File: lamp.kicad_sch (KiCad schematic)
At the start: 18 parts, among them J1 Screw_Terminal_01x02, J2 Screw_Terminal_01x02, Q1 2N7002, U1 ESP-12E, U2 34.81-7048, U3 AMS1117-3.3

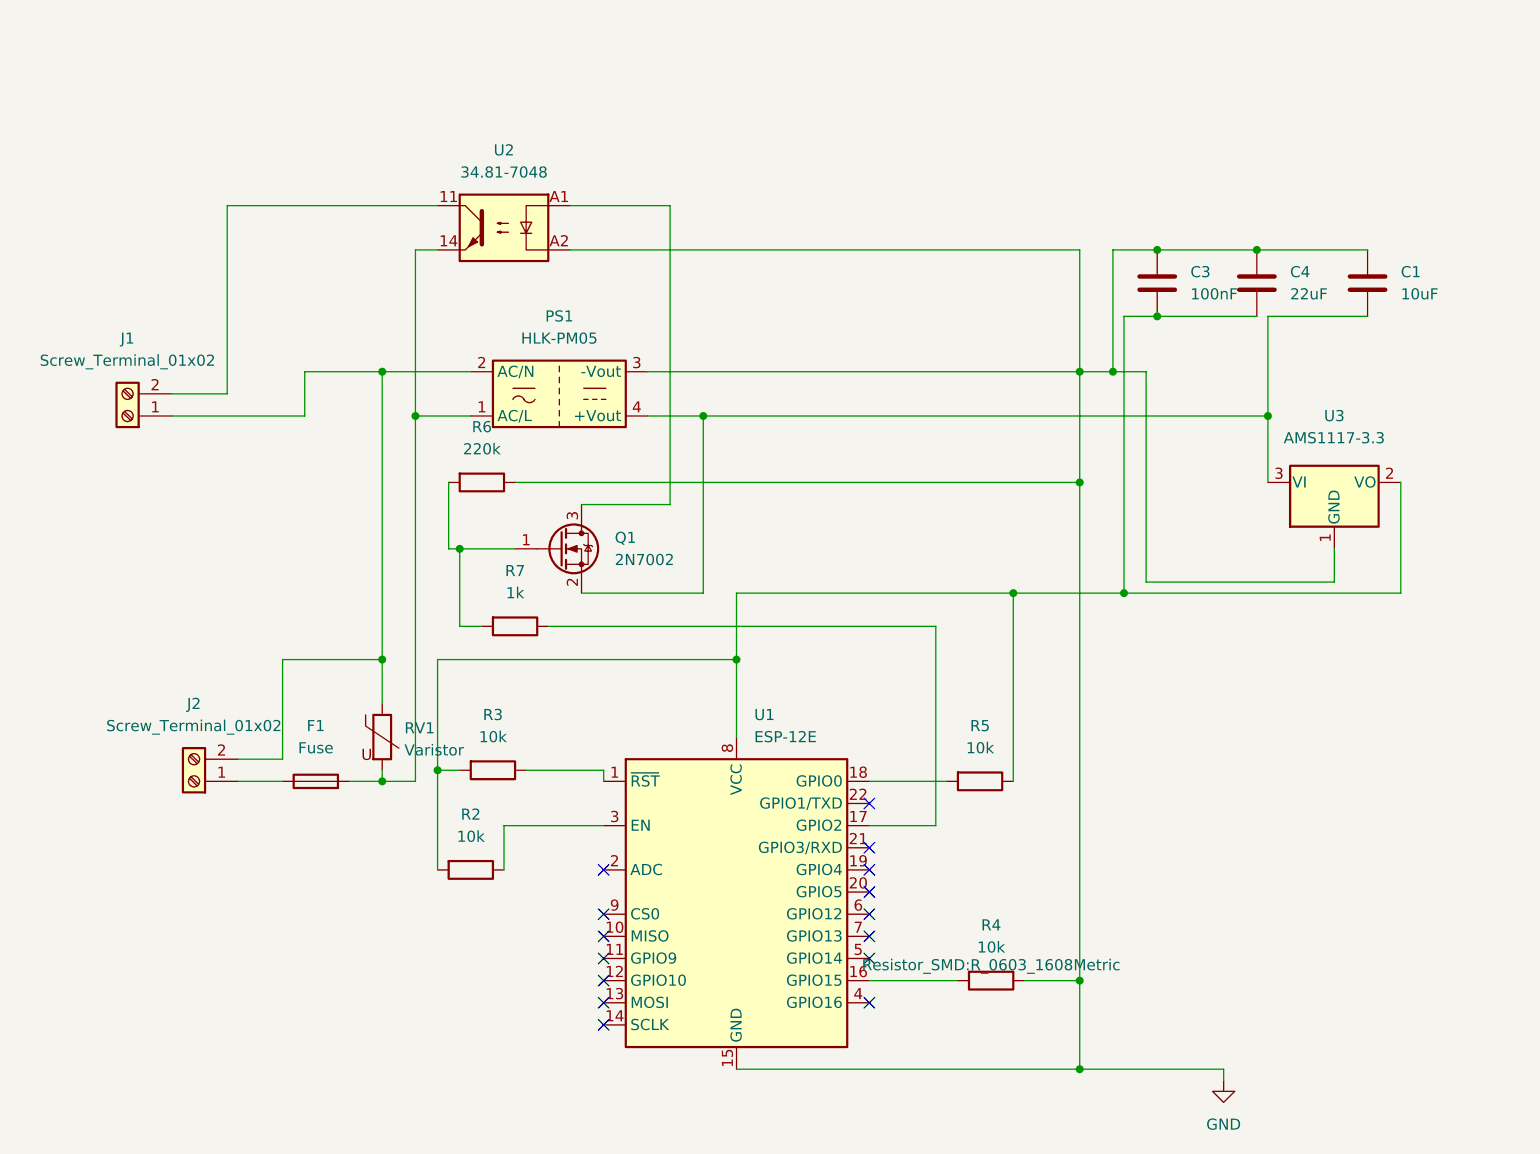
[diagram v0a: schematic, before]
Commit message: 0.1 revision
broken tracing
fixed capacitor footprint
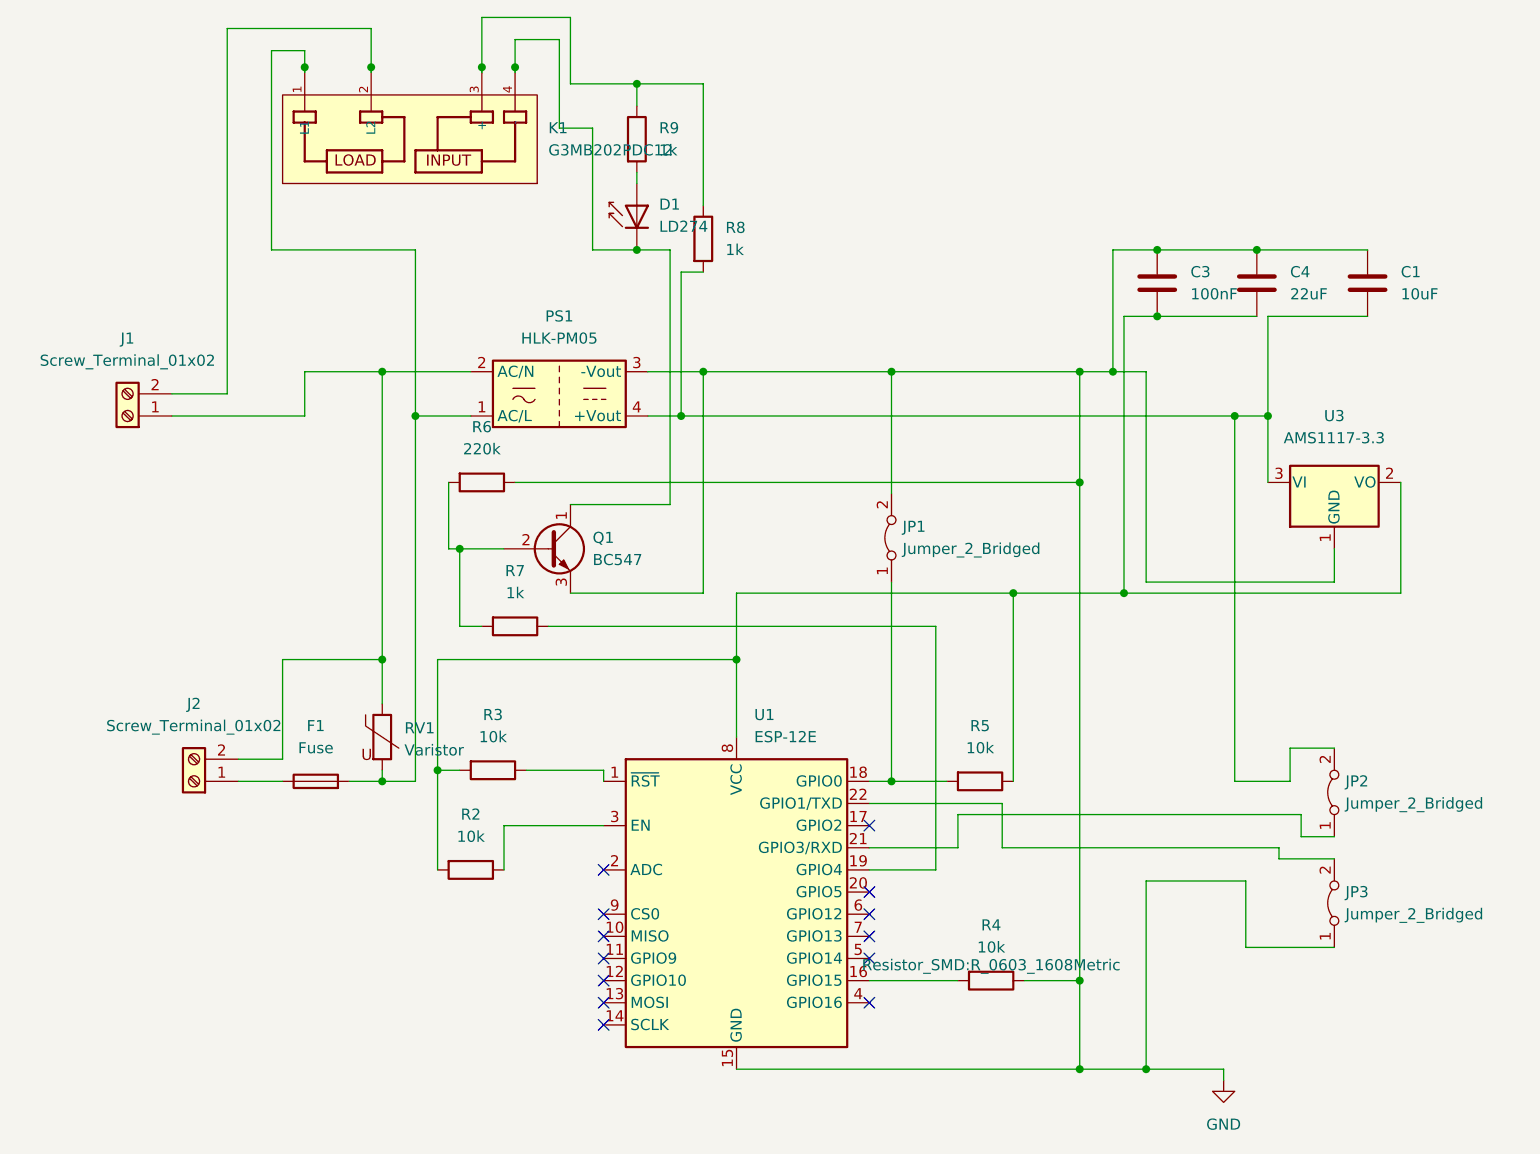
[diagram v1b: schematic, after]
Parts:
- removed Q1: 2N7002, Package_TO_SOT_SMD:SOT-23, symbol Transistor_FET:2N7002
- removed U2: 34.81-7048, OptoDevice:Finder_34.81, symbol Relay_SolidState:34.81-7048
- added D1: LD274, LED_THT:LED_D5.0mm_IRGrey, symbol LED:LD274
- added JP1, JP2, JP3: Jumper_2_Bridged, TestPoint:TestPoint_2Pads_Pitch2.54mm_Drill0.8mm, symbol Jumper:Jumper_2_Bridged
- added K1: G3MB202PDC12, G3MB202PDC12:RELAY_G3MB202PDC12, symbol G3MB202PDC12:G3MB202PDC12
- added Q1: BC547, Package_TO_SOT_THT:TO-92_Inline, symbol Transistor_BJT:BC547
- added R8, R9: 1k, Resistor_SMD:R_0603_1608Metric, symbol Device:R
- C1, C3, C4: footprint Capacitor_Tantalum_SMD:CP_EIA-3216-18_Kemet-A_Pad1.58x1.35mm_HandSolder -> Capacitor_THT:CP_Radial_D5.0mm_P2.50mm
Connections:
- net GND: now also JP1.2 (B), JP3.1 (A), Q1.3 (E)
- net at F1.2, PS1.1 (AC/L), RV1.2: now also K1.1 (L1)
- net at C1.2, PS1.4 (+Vout), U3.3 (VI): now also JP2.2 (B), R8.2
- net at R5.2, U1.18 (GPIO0): now also JP1.1 (A)
- net at J1.2 (Pin_2): now also K1.2 (L2)
- net at R7.1: now also U1.19 (GPIO4); no longer U1.17 (GPIO2)
- net at R6.2, R7.2: now also Q1.2 (B)
- net at U1.21 (GPIO3/RXD): now also JP2.1 (A)
- net at U1.22 (GPIO1/TXD): now also JP3.2 (B)
- new net: D1.1 (K), K1.4 (-), Q1.1 (C)
- new net: K1.3 (+), R8.1, R9.1
- new net: D1.2 (A), R9.2
- no-connect marks 15 -> 13

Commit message: updated v0.0.1A
update
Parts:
- removed JP2, JP3: Jumper_2_Bridged, TestPoint:TestPoint_2Pads_Pitch2.54mm_Drill0.8mm, symbol Jumper:Jumper_2_Bridged
- added J3: Conn_01x04_Pin, Connector_PinHeader_2.54mm:PinHeader_1x04_P2.54mm_Vertical, symbol Connector:Conn_01x04_Pin
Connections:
- net GND: now also J3.1 (Pin_1)
- net at C1.2, PS1.4 (+Vout), R8.2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: now also J3.4 (Pin_4)
- net at U1.22 (GPIO1/TXD): now also J3.3 (Pin_3)
- net at U1.21 (GPIO3/RXD): now also J3.2 (Pin_2)
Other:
- moved on the sheet: R2, R3
